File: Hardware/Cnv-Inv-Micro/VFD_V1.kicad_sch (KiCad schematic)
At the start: 0 parts

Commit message: Normalizacion placa micros
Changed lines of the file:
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@@
 	(paper "A4")
 	(sheet
-		(at 101.6 40.64)
+		(at 124.46 33.02)
 		(size 45.72 33.02)
 		(exclude_from_sim no)
@@
 		)
 		(property "Sheetname" "Micro"
-			(at 101.6 39.9284 0)
+			(at 124.46 32.3084 0)
 			(effects
 				(font
@@
 		)
 		(property "Sheetfile" "micro.kicad_sch"
-			(at 101.6 74.2446 0)
+			(at 124.46 66.6246 0)
 			(effects
 				(font
@@
 	)
 	(sheet
-		(at 185.42 91.44)
-		(size 68.58 38.1)
+		(at 182.88 86.36)
+		(size 52.07 29.21)
 		(exclude_from_sim no)
 		(in_bom yes)
@@
 		)
 		(property "Sheetname" "Inversor"
-			(at 185.42 90.7284 0)
+			(at 182.88 85.6484 0)
 			(effects
 				(font
@@
 		)
 		(property "Sheetfile" "inversor.kicad_sch"
-			(at 185.42 130.1246 0)
+			(at 182.88 116.1546 0)
 			(effects
 				(font
@@
 	)
 	(sheet
-		(at 55.88 93.98)
+		(at 62.23 83.82)
 		(size 53.34 30.48)
 		(exclude_from_sim no)
@@
 		)
 		(property "Sheetname" "Conversor"
-			(at 55.88 93.2684 0)
+			(at 62.23 83.1084 0)
 			(effects
 				(font
@@
 		)
 		(property "Sheetfile" "conversor.kicad_sch"
-			(at 55.88 125.0446 0)
+			(at 62.23 114.8846 0)
 			(effects
 				(font

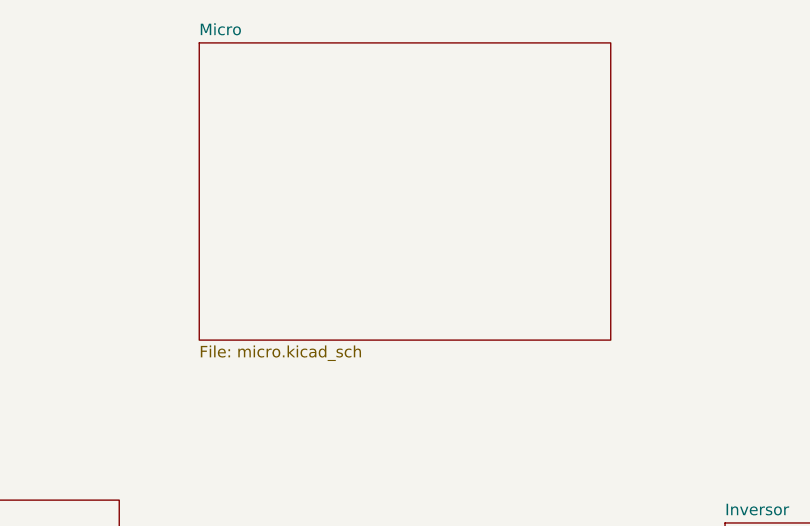
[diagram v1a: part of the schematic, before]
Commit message: Avances en PCB conversor y inversor - Simulaciones de modulacion
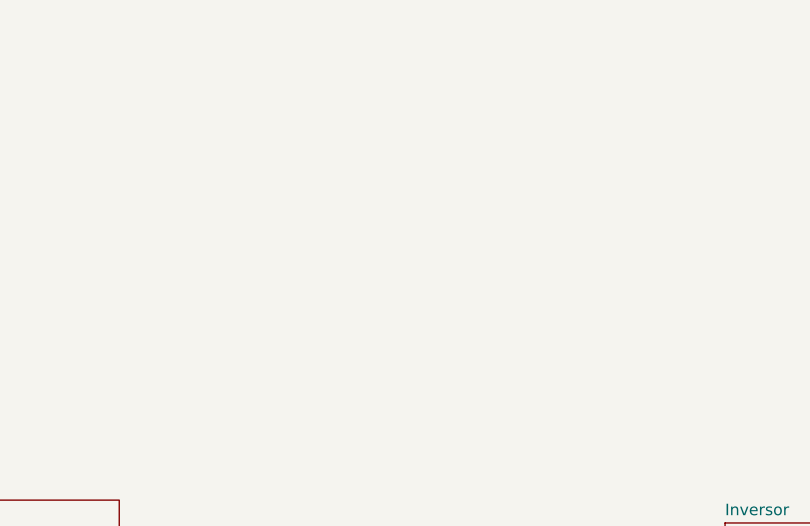
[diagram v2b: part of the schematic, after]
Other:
- removed sheet Micro
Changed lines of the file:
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@@
 	(paper "A4")
-	(sheet
-		(at 124.46 33.02)
-		(size 45.72 33.02)
-		(exclude_from_sim no)
-		(in_bom yes)
-		(on_board yes)
-		(dnp no)
-		(fields_autoplaced yes)
-		(stroke
-			(width 0.1524)
-			(type solid)
-		)
-		(fill
-			(color 0 0 0 0.0000)
-		)
-		(property "Sheetname" "Micro"
-			(at 124.46 32.3084 0)
-			(effects
-				(font
-					(size 1.27 1.27)
-				)
-				(justify left bottom)
-			)
-		)
-		(property "Sheetfile" "micro.kicad_sch"
-			(at 124.46 66.6246 0)
-			(effects
-				(font
-					(size 1.27 1.27)
-				)
-				(justify left top)
-			)
-		)
-		(instances
-			(project "VFD_V1"
-				(path "/e60c11d9-ab9e-4760-a4a7-008fcec65a72"
-					(page "4")
-				)
-			)
-		)
-	)
 	(sheet
 		(at 182.88 86.36)
